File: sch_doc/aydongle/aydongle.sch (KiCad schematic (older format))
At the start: 53 parts, among them J1 prog, J2 USB_A, J3 Display, J4 Audio-Jack-3, Q1 Q_Photo_NPN_EC, Q2 Q_Photo_NPN_CE, U1 AP1117-33, U2 STM32F103C8TxSmall, U3 YM2149F, U4 LM4811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

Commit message: доделал схему, надеюсь окончательный вариант
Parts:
- removed C25: 0.1uF, Capacitor_SMD:C_0603_1608Metric, symbol device:C
- removed R13: 560k, Resistor_SMD:R_0805_2012Metric, symbol device:R
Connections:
- net D_RST: now reaches U2.41 (PB5)
- net D_RST: now also J3.9 (Pin_9)
- no-connect marks 27 -> 26
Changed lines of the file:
@@
 EESchema Schematic File Version 4
-LIBS:aydongle-cache
 EELAYER 30 0
 EELAYER END
@@
 Wire Wire Line
 	1750 1400 1800 1400
-NoConn ~ 4000 3800
 Wire Wire Line
 	10050 5200 10000 5200
@@
 Wire Wire Line
 	10000 4900 10050 4900
-$Comp
-L device:R R13
-U 1 1 5DF6ECCA
-P 9700 5150
-F 0 "R13" V 9650 5000 50  0000 C CNN
-F 1 "560k" V 9700 5150 50  0000 C CNN
-F 2 "Resistor_SMD:R_0805_2012Metric" V 9630 5150 50  0001 C CNN
-F 3 "" H 9700 5150 50  0001 C CNN
-	1    9700 5150
-	0    1    1    0
-$EndComp
-$Comp
-L device:C C25
-U 1 1 5DF6F9D8
-P 9700 5300
-F 0 "C25" H 9800 5400 50  0000 R CNN
-F 1 "0.1uF" H 9800 5200 50  0000 R CNN
-F 2 "Capacitor_SMD:C_0603_1608Metric" H 9738 5150 50  0001 C CNN
-F 3 "" H 9700 5300 50  0001 C CNN
-	1    9700 5300
-	0    -1   -1   0
-$EndComp
-Wire Wire Line
-	9850 5300 9900 5300
-Wire Wire Line
-	9850 5150 9900 5150
-Wire Wire Line
-	9900 5150 9900 5300
-Connection ~ 9900 5300
-Wire Wire Line
-	9900 5300 10050 5300
 Wire Wire Line
 	10050 5500 9200 5500
 Wire Wire Line
-	10050 5100 9950 5100
-Wire Wire Line
-	9950 5100 9950 5550
-Wire Wire Line
 	9500 6250 9500 6150
-Wire Wire Line
-	9500 5550 9950 5550
 Wire Wire Line
 	9650 5600 9500 5600
 Connection ~ 9500 5600
 Wire Wire Line
-	9500 5600 9500 5550
-Wire Wire Line
 	9500 5750 9650 5750
 Connection ~ 9500 5750
@@
 	9500 6150 9500 5950
 Wire Wire Line
-	9500 5550 9500 5300
-Wire Wire Line
-	9500 5300 9550 5300
-Connection ~ 9500 5550
-Wire Wire Line
-	9550 5150 9500 5150
-Wire Wire Line
 	9500 4900 10000 4900
 Wire Wire Line
 	9500 4900 9500 4400
-Connection ~ 9500 4900
 $Comp
 L device:R R12
@@
 Wire Wire Line
 	9000 950  9000 2050
-Wire Wire Line
-	9500 4900 9500 5150
 $Comp
 L device:LED D3
@@
 	-1   0    0    1
 $EndComp
-Text Label 3700 2900 0    50   ~ 0
-GND
 Wire Wire Line
 	1450 1450 1450 1400
@@
 Entry Wire Line
 	3600 4800 3700 4700
+Text Label 3700 3800 0    50   ~ 0
+D_RST
+Entry Wire Line
+	9100 5400 9200 5300
+Wire Wire Line
+	9500 5100 10050 5100
+Wire Wire Line
+	9500 5100 9500 5600
+Text Label 9250 5300 0    50   ~ 0
+D_RST
+Wire Wire Line
+	9200 5300 10050 5300
+Wire Wire Line
+	4000 3800 3700 3800
 Wire Bus Line
 	3700 5800 9200 5800
@@
 Wire Bus Line
 	3600 3000 3600 6650
+Entry Wire Line
+	3600 3900 3700 3800
+Text Label 3700 2900 0    50   ~ 0
+GND
 $EndSCHEMATC

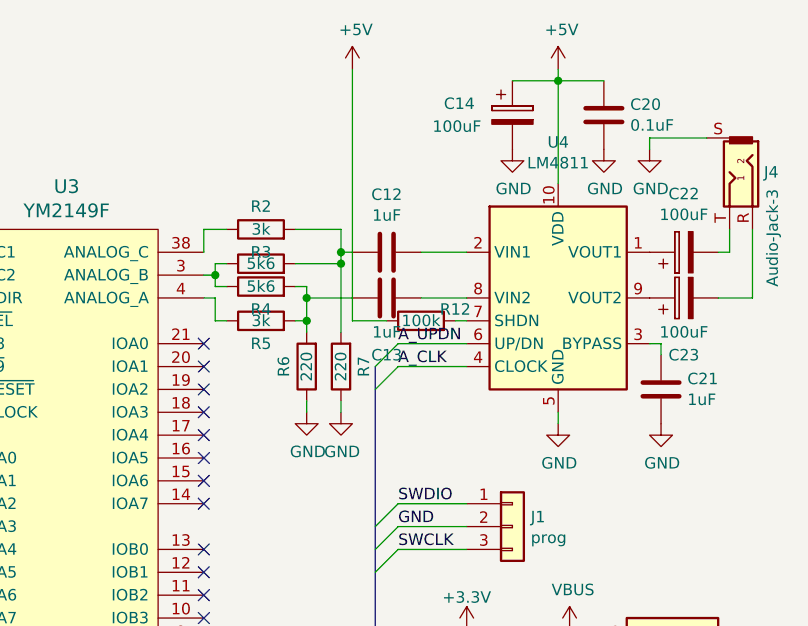
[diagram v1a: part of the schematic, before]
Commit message: работает чип и усилитель
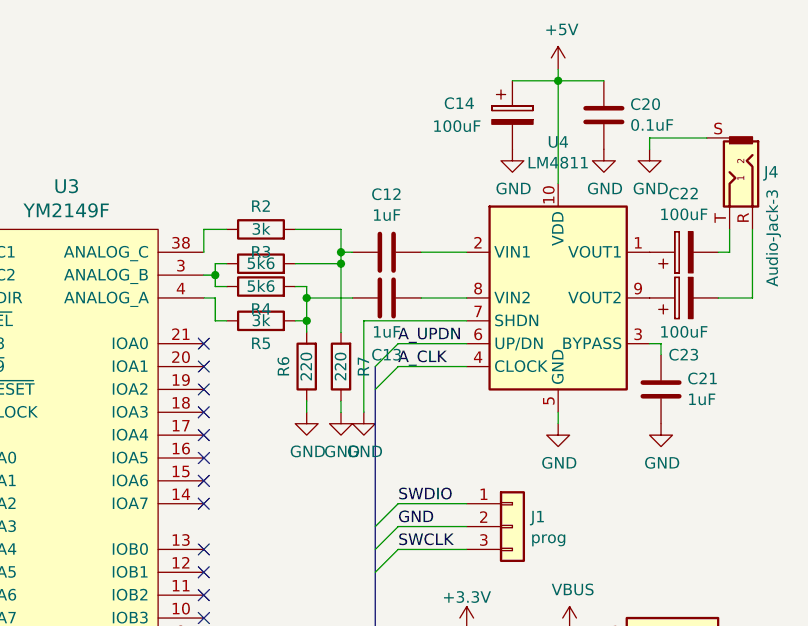
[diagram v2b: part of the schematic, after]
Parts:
- removed R12: 100k, Resistor_SMD:R_0805_2012Metric, symbol device:R
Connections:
- net GND: now also U4.7 (SHDN)
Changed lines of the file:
@@
 Wire Wire Line
 	9500 4900 9500 4400
-$Comp
-L device:R R12
-U 1 1 5E148781
-P 9300 2050
-F 0 "R12" V 9350 1900 50  0000 C CNN
-F 1 "100k" V 9300 2050 50  0000 C CNN
-F 2 "Resistor_SMD:R_0805_2012Metric" V 9230 2050 50  0001 C CNN
-F 3 "" H 9300 2050 50  0001 C CNN
-	1    9300 2050
-	0    -1   -1   0
-$EndComp
-Wire Wire Line
-	9500 2050 9450 2050
-$Comp
-L power:+5V #PWR01
-U 1 1 5E15D7CC
-P 9000 950
-F 0 "#PWR01" H 9000 800 50  0001 C CNN
-F 1 "+5V" H 9015 1123 50  0000 C CNN
-F 2 "" H 9000 950 50  0001 C CNN
-F 3 "" H 9000 950 50  0001 C CNN
-	1    9000 950
-	1    0    0    -1
-$EndComp
-Wire Wire Line
-	9150 2050 9000 2050
 Wire Wire Line
 	8950 1750 8950 1800
@@
 Wire Wire Line
 	9000 1750 8950 1750
-Wire Wire Line
-	9000 950  9000 2050
 $Comp
 L device:LED D3
@@
 Wire Wire Line
 	4000 3800 3700 3800
-Wire Bus Line
-	3700 5800 9200 5800
-Wire Bus Line
-	9100 2250 9100 5700
-Wire Bus Line
-	6800 1850 6800 5700
-Wire Bus Line
-	6100 3400 6100 5700
-Wire Bus Line
-	3600 3000 3600 6650
 Entry Wire Line
 	3600 3900 3700 3800
 Text Label 3700 2900 0    50   ~ 0
 GND
+$Comp
+L power:GND #PWR0137
+U 1 1 5EBEF025
+P 9050 2450
+F 0 "#PWR0137" H 9050 2200 50  0001 C CNN
+F 1 "GND" H 9055 2277 50  0000 C CNN
+F 2 "" H 9050 2450 50  0001 C CNN
+F 3 "" H 9050 2450 50  0001 C CNN
+	1    9050 2450
+	1    0    0    -1
+$EndComp
+Wire Wire Line
+	9050 2450 9050 2050
+Wire Wire Line
+	9050 2050 9500 2050
+Wire Bus Line
+	3700 5800 9200 5800
+Wire Bus Line
+	9100 2250 9100 5700
+Wire Bus Line
+	6800 1850 6800 5700
+Wire Bus Line
+	6100 3400 6100 5700
+Wire Bus Line
+	3600 3000 3600 6650
 $EndSCHEMATC
